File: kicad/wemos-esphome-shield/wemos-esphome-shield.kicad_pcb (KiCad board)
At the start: 2 copper layers, 88.5 x 54 mm, 21 parts, among them Q1 2N2219, Q2 2N2219, T1 Transformer_1P_1S, U1 WeMos_D1_mini

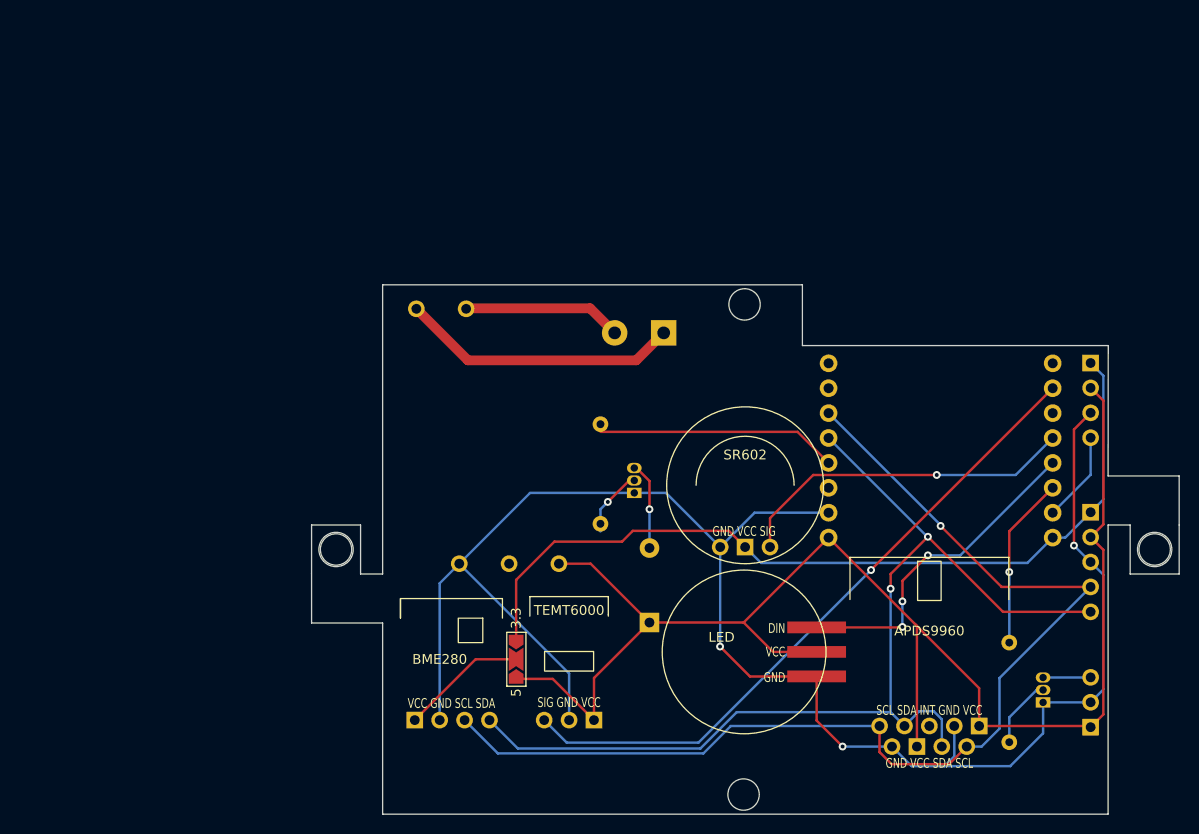
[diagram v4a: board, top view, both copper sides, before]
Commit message: add oled screen pads
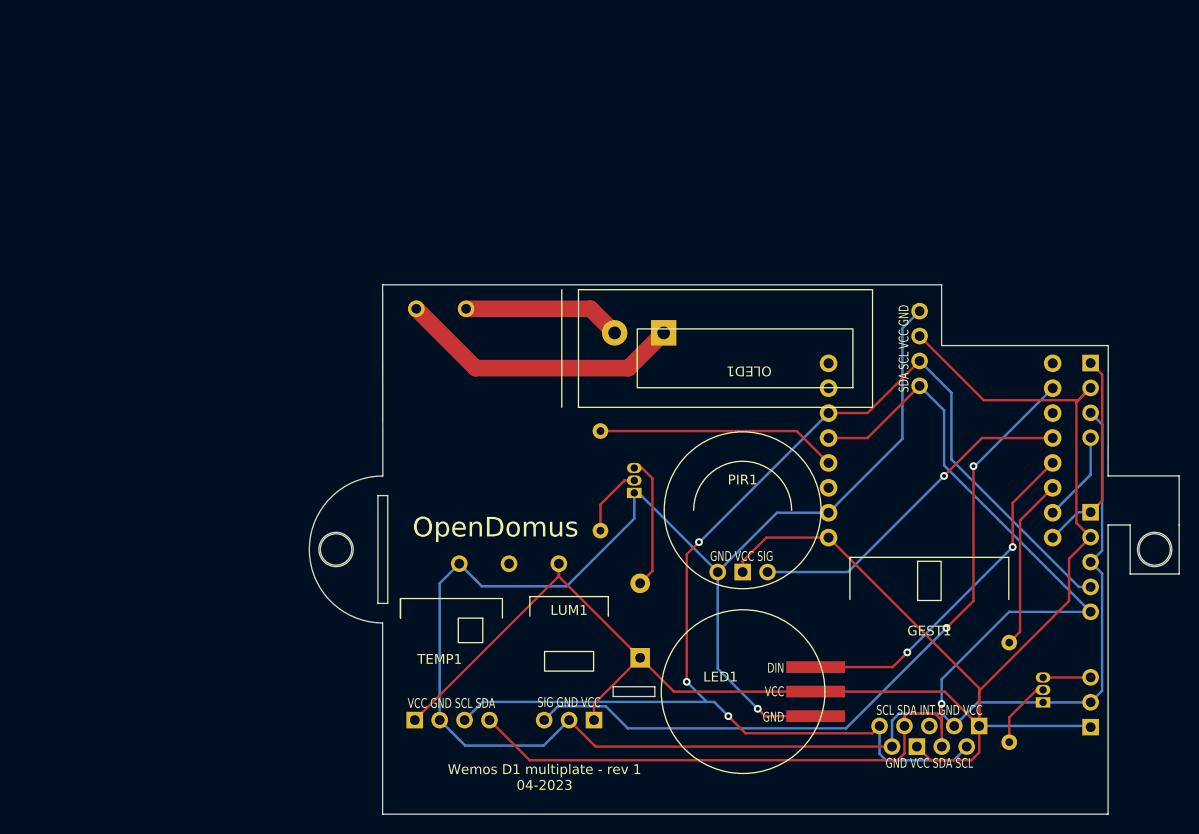
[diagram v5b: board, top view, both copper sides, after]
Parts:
- removed H3, H4: MountingHole, MountingHole:MountingHole_3.2mm_M3
- removed JP1: SolderJumper_3_Open, Jumper:SolderJumper-3_P2.0mm_Open_TrianglePad1.0x1.5mm_NumberLabels
- added OLED1: Conn_01x04_Female, internal:SSD1306 OLED 128x32, F.Cu at (133.8, 70.5)
- moved LED1 4.05 mm to (115.8, 105.5)
- moved BZ1 3.72 mm to (105.2, 102.0)
- moved PIR1 2.56 mm to (115.7, 93.3)
- moved R1 0.70 mm to (101.2, 78.9)
- renumbered APDS9960 to GEST1, LED to LED1, TEMT6000 to LUM1, SR602 to PIR1, BME280 to TEMP1
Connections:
- PIR1 pad 2: 3.3V -> 5V
- TEMP1 pad 1: Net-(BME1-Pad1) -> 5V
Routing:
- net 3.3V: track 86.6 -> 21.1 mm
- net 5V: track 150.6 -> 199.6 mm
- net GND: track 178.5 -> 218.6 mm, vias 3 -> 1
- net SCL: track 114.2 -> 136.1 mm, vias 1 -> 3
- net SDA: track 106.8 -> 119.8 mm, vias 2 -> 1
- net Net-(BME1-Pad1): track 12.9 -> 0.00 mm
- net A0: track 67.8 -> 75.8 mm, vias 1 -> 2
- net Net-(BZ1-Pad2): track 8.93 -> 13.5 mm, vias 1 -> 0
- net D6: track 33.8 -> 35.4 mm, vias 3 -> 2
- net L: track 28.6 -> 29.2 mm
- net Net-(Q1-Pad2): track 6.93 -> 7.13 mm, vias 1 -> 0
- net D7: track 17.5 -> 17.6 mm, vias 1 -> 0
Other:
- board size 88.5 x 54 mm -> 88.7 x 54 mm
- board text added: "OpenDomus"
- board text added: "Wemos D1 multiplate - rev 1 04-2023"

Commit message: fix logos
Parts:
- added G***: LOGO, LOGO, F.Cu at (90.0, 78.0)
- added G***: LOGO, LOGO, B.Cu at (117.8, 105.8)
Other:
- outline, holes or cut-outs redrawn

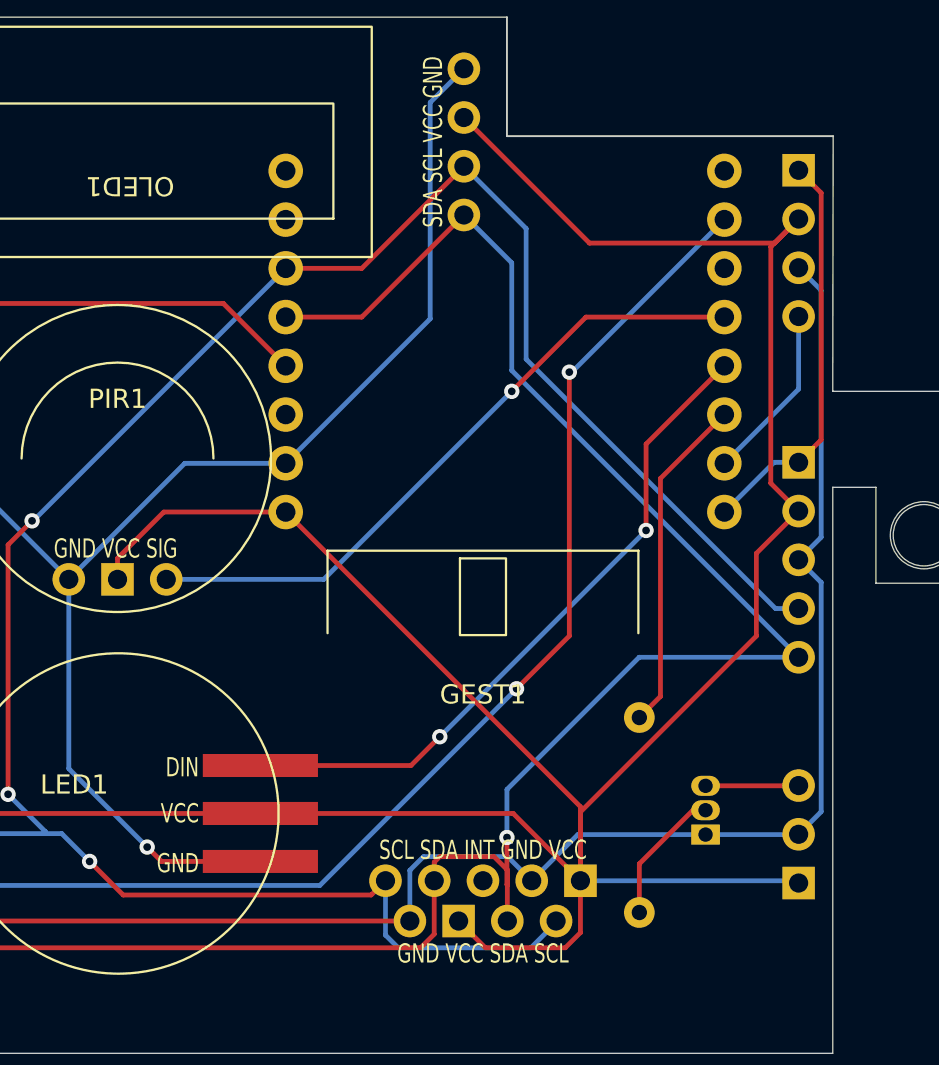
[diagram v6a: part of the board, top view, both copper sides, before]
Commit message: fix schema and routing for APDS9960
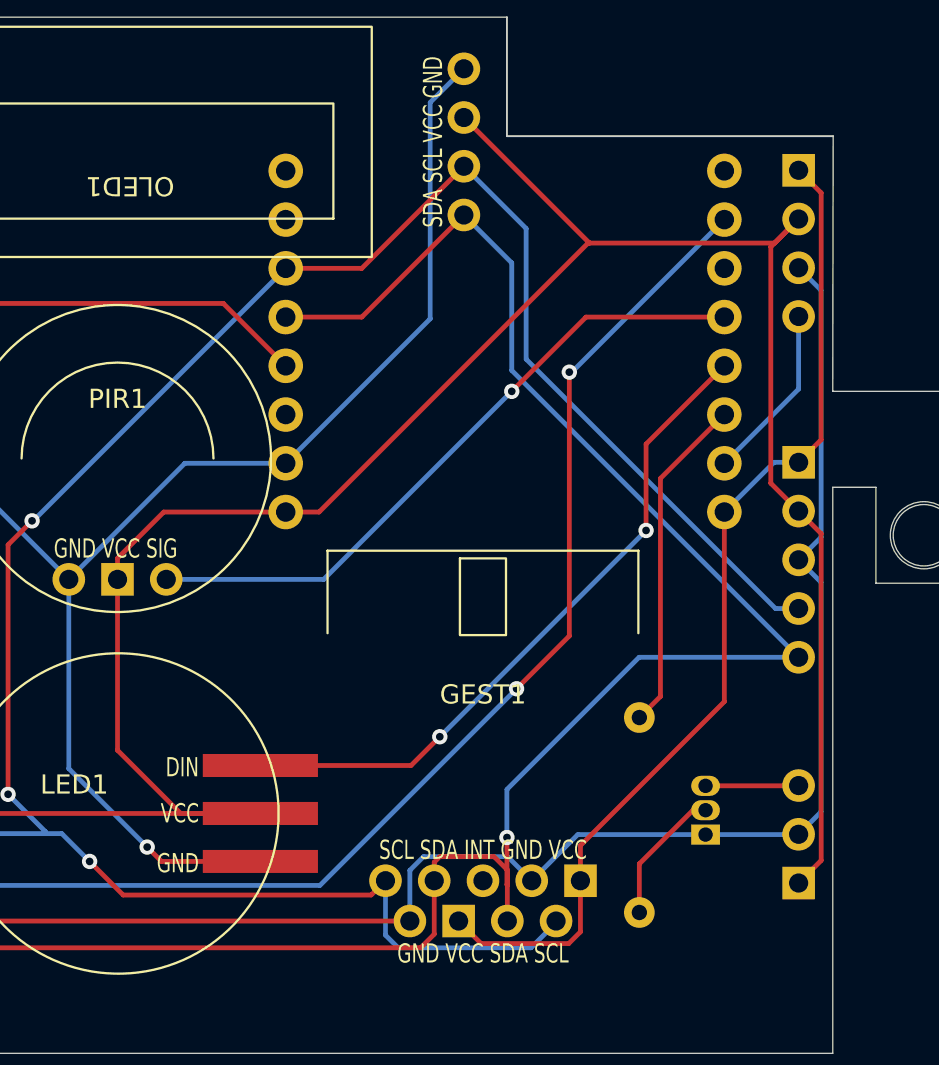
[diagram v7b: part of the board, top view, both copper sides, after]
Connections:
- GEST1 pad 5: 5V -> 3.3V
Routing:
- net 3.3V: track 21.1 -> 53.2 mm
- net 5V: track 199.6 -> 170.4 mm
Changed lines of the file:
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@@
       (net 7 "GND") (pinfunction "Pin_4") (pintype "passive"))
     (pad "5" thru_hole rect (at -1.27 2.1) (size 1.7 1.7) (drill 1) (layers *.Cu *.Mask)
-      (net 1 "5V") (pinfunction "Pin_5") (pintype "passive"))
+      (net 6 "3.3V") (pinfunction "Pin_5") (pintype "passive"))
     (pad "5" thru_hole rect (at 5.08 0) (size 1.7 1.7) (drill 1) (layers *.Cu *.Mask)
-      (net 1 "5V") (pinfunction "Pin_5") (pintype "passive"))
+      (net 6 "3.3V") (pinfunction "Pin_5") (pintype "passive"))
   )
   (footprint "MountingHole:MountingHole_3.2mm_M3" (layer "F.Cu")
@@
   (segment (start 149.75 75.97) (end 149.75 88.29) (width 0.25) (layer "F.Cu") (net 1))
   (segment (start 115.704688 93.3) (end 115.704688 92.2) (width 0.25) (layer "F.Cu") (net 1))
+  (segment (start 151.2 89.74) (end 152.375 90.915) (width 0.25) (layer "F.Cu") (net 1))
+  (segment (start 152.375 107.95) (end 151.2 109.125) (width 0.25) (layer "F.Cu") (net 1))
   (segment (start 149.945 75.775) (end 151.2 74.52) (width 0.25) (layer "F.Cu") (net 1))
   (segment (start 149.75 88.29) (end 151.2 89.74) (width 0.25) (layer "F.Cu") (net 1))
-  (segment (start 139.83 109.005) (end 139.83 111.708351) (width 0.25) (layer "F.Cu") (net 1))
   (segment (start 96.96 92.45) (end 96.96 93.705) (width 0.25) (layer "F.Cu") (net 1))
-  (segment (start 139.83 105.42) (end 139.83 109.005) (width 0.25) (layer "F.Cu") (net 1))
   (segment (start 96.96 93.76) (end 105.25 102.05) (width 0.25) (layer "F.Cu") (net 1))
+  (segment (start 140.2625 75.7375) (end 140.3 75.775) (width 0.25) (layer "F.Cu") (net 1))
   (segment (start 118.114688 89.79) (end 124.47 89.79) (width 0.25) (layer "F.Cu") (net 1))
-  (segment (start 151.2 89.74) (end 149 91.94) (width 0.25) (layer "F.Cu") (net 1))
-  (segment (start 133.755 69.23) (end 140.3 75.775) (width 0.25) (layer "F.Cu") (net 1))
-  (segment (start 136.325 105.5) (end 139.83 109.005) (width 0.25) (layer "F.Cu") (net 1))
+  (segment (start 152.375 90.915) (end 152.375 107.95) (width 0.25) (layer "F.Cu") (net 1))
+  (segment (start 119 105.5) (end 115.704688 102.204688) (width 0.25) (layer "F.Cu") (net 1))
   (segment (start 151.2 74.52) (end 149.75 75.97) (width 0.25) (layer "F.Cu") (net 1))
+  (segment (start 123.15 105.5) (end 119 105.5) (width 0.25) (layer "F.Cu") (net 1))
   (segment (start 96.96 93.705) (end 82.26 108.405) (width 0.25) (layer "F.Cu") (net 1))
-  (segment (start 139.83 109.005) (end 139.83 105.15) (width 0.25) (layer "F.Cu") (net 1))
-  (segment (start 123.15 105.5) (end 136.325 105.5) (width 0.25) (layer "F.Cu") (net 1))
+  (segment (start 133.755 69.23) (end 140.2625 75.7375) (width 0.25) (layer "F.Cu") (net 1))
   (segment (start 108.7 105.5) (end 123.15 105.5) (width 0.25) (layer "F.Cu") (net 1))
-  (segment (start 139.038351 112.5) (end 134.875 112.5) (width 0.25) (layer "F.Cu") (net 1))
   (segment (start 105.25 102.05) (end 100.54 106.76) (width 0.25) (layer "F.Cu") (net 1))
   (segment (start 115.704688 92.2) (end 118.114688 89.79) (width 0.25) (layer "F.Cu") (net 1))
   (segment (start 100.54 106.76) (end 100.54 108.405) (width 0.25) (layer "F.Cu") (net 1))
-  (segment (start 139.83 111.708351) (end 139.038351 112.5) (width 0.25) (layer "F.Cu") (net 1))
-  (segment (start 139.83 105.15) (end 124.47 89.79) (width 0.25) (layer "F.Cu") (net 1))
-  (segment (start 149 91.94) (end 149 96.25) (width 0.25) (layer "F.Cu") (net 1))
+  (segment (start 124.47 89.79) (end 126.21 89.79) (width 0.25) (layer "F.Cu") (net 1))
+  (segment (start 126.21 89.79) (end 140.2625 75.7375) (width 0.25) (layer "F.Cu") (net 1))
+  (segment (start 115.704688 102.204688) (end 115.704688 93.3) (width 0.25) (layer "F.Cu") (net 1))
   (segment (start 96.96 92.45) (end 96.96 93.76) (width 0.25) (layer "F.Cu") (net 1))
   (segment (start 140.3 75.775) (end 149.945 75.775) (width 0.25) (layer "F.Cu") (net 1))
   (segment (start 105.25 102.05) (end 108.7 105.5) (width 0.25) (layer "F.Cu") (net 1))
-  (segment (start 134.875 112.5) (end 133.48 111.105) (width 0.25) (layer "F.Cu") (net 1))
-  (segment (start 149 96.25) (end 139.83 105.42) (width 0.25) (layer "F.Cu") (net 1))
-  (segment (start 139.83 109.005) (end 151.08 109.005) (width 0.25) (layer "B.Cu") (net 1))
   (segment (start 89.88 108.405) (end 93.975 112.5) (width 0.25) (layer "F.Cu") (net 2))
   (segment (start 93.975 112.5) (end 131.5 112.5) (width 0.25) (layer "F.Cu") (net 2))
@@
   (segment (start 151.2 83.38) (end 151.2 79.6) (width 0.25) (layer "B.Cu") (net 5))
   (segment (start 147.33 87.25) (end 151.2 83.38) (width 0.25) (layer "B.Cu") (net 5))
+  (segment (start 133.48 111.105) (end 134.655 112.28) (width 0.25) (layer "F.Cu") (net 6))
+  (segment (start 139.22 112.28) (end 139.83 111.67) (width 0.25) (layer "F.Cu") (net 6))
+  (segment (start 134.655 112.28) (end 139.22 112.28) (width 0.25) (layer "F.Cu") (net 6))
+  (segment (start 139.83 111.67) (end 139.83 109.005) (width 0.25) (layer "F.Cu") (net 6))
+  (segment (start 147.33 99.67) (end 147.33 89.79) (width 0.25) (layer "F.Cu") (net 6))
   (segment (start 152.375 86.025) (end 151.2 87.2) (width 0.25) (layer "F.Cu") (net 6))
   (segment (start 152.375 73.155) (end 152.375 86.025) (width 0.25) (layer "F.Cu") (net 6))
   (segment (start 151.2 71.98) (end 152.375 73.155) (width 0.25) (layer "F.Cu") (net 6))
+  (segment (start 139.83 109.005) (end 139.83 107.17) (width 0.25) (layer "F.Cu") (net 6))
+  (segment (start 139.83 107.17) (end 147.33 99.67) (width 0.25) (layer "F.Cu") (net 6))
   (segment (start 147.33 89.79) (end 149.92 87.2) (width 0.25) (layer "B.Cu") (net 6))
   (segment (start 149.92 87.2) (end 151.2 87.2) (width 0.25) (layer "B.Cu") (net 6))

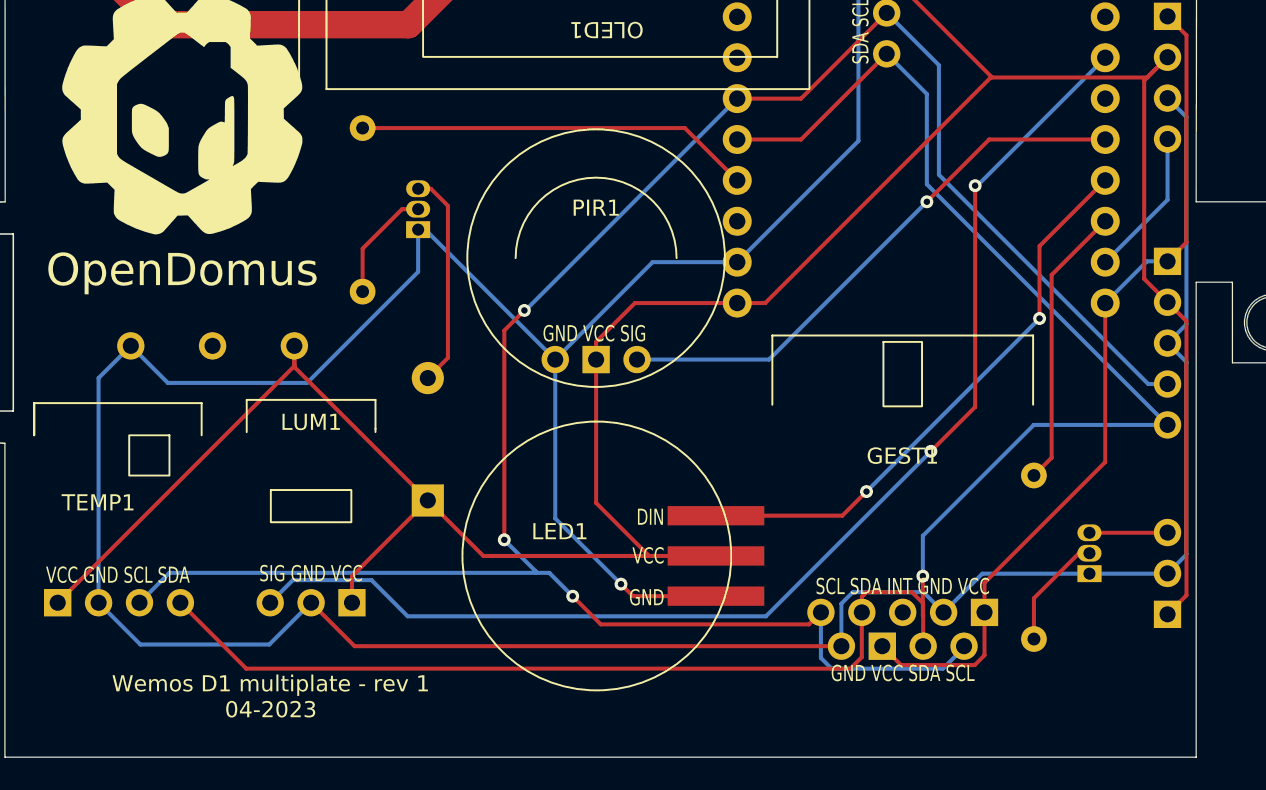
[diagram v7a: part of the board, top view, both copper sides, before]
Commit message: fix schema and routing for apds9960
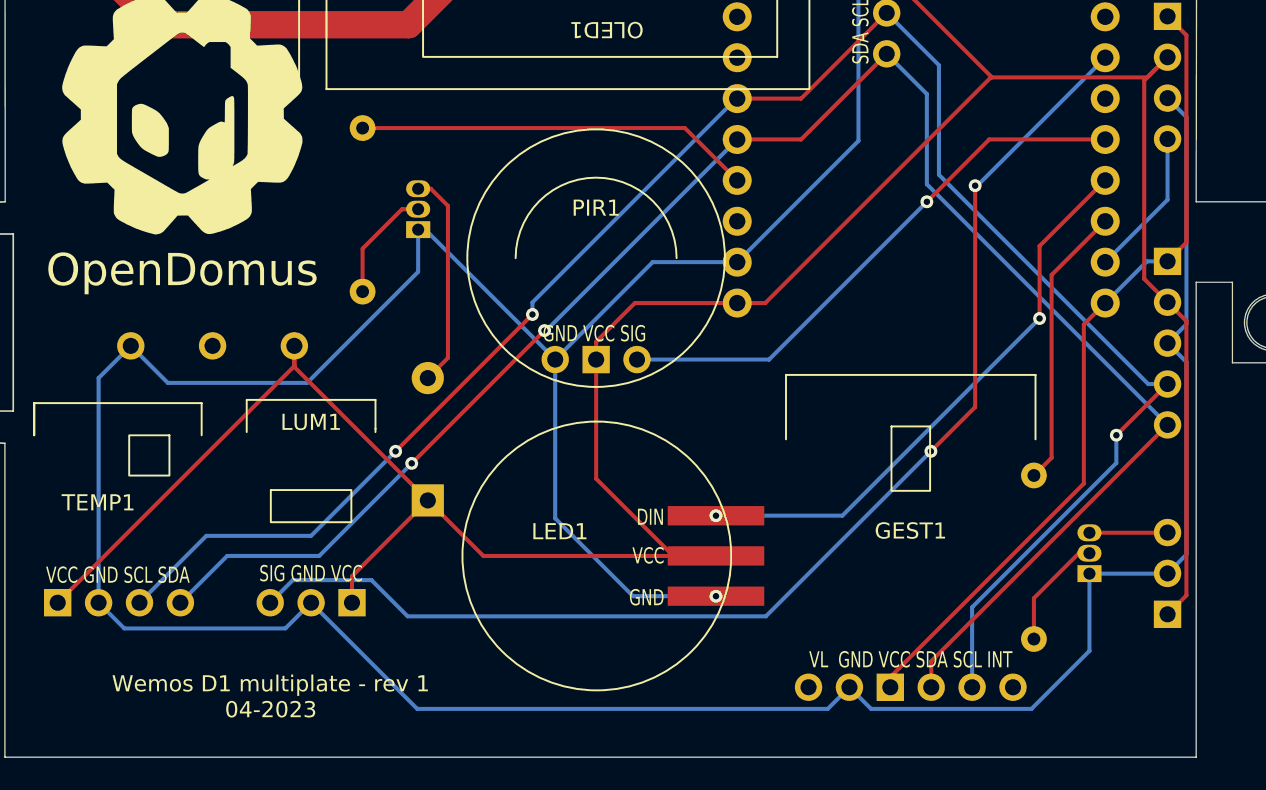
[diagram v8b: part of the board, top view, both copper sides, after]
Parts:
- GEST1: footprint internal:APDS9960 double pinout -> internal:APDS9960
- moved GEST1 4.68 mm to (135.2, 113.7)
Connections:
- GEST1 pad 1: SCL -> unconnected-(GEST1-Pad1)
- GEST1 pad 2: SDA -> GND
- GEST1 pad 3: unconnected-(GEST1-Pad3) -> 3.3V
- GEST1 pad 4: GND -> SDA
- GEST1 pad 5: 3.3V -> SCL
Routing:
- net SCL: track 136.1 -> 116.9 mm
- net SDA: track 119.8 -> 110.6 mm, vias 1 -> 2
- net GND: track 218.6 -> 222.3 mm
- net 3.3V: track 53.2 -> 50.5 mm
- net 5V: track 170.4 -> 169.5 mm
